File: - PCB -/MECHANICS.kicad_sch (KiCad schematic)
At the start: 7 parts, among them SW1 SW_SPDT, SW3 SW_Push

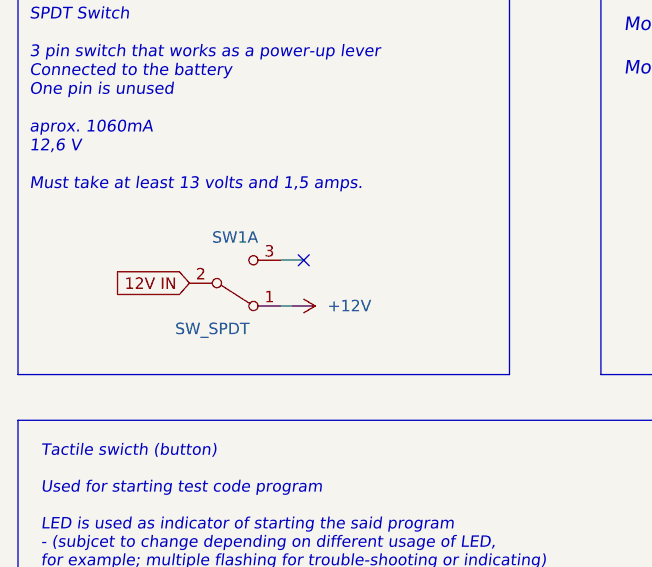
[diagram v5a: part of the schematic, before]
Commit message: PCB almost wired
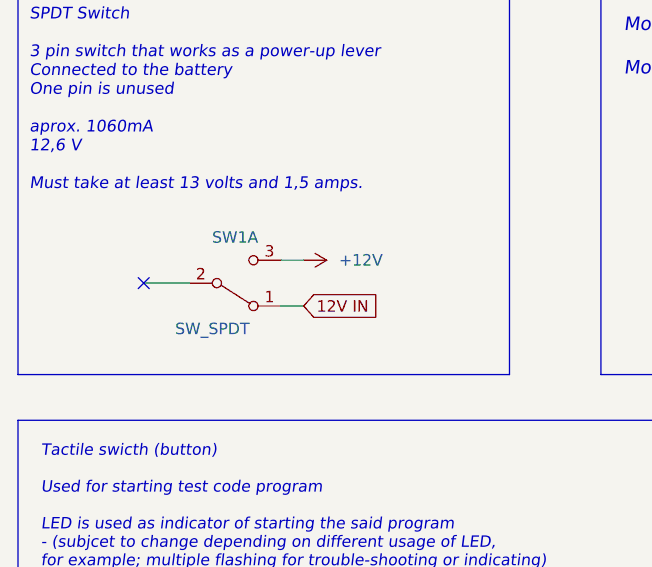
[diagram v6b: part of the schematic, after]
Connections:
- net +12V: now also SW1.3 (C); no longer SW1.1 (A)
- net 12V IN: now also SW1.1 (A); no longer SW1.2 (B)
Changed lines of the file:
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@@
   (junction (at 173.99 139.7) (diameter 0) (color 0 0 0 0)
   )
-  (no_connect (at 97.79 97.79))
+  (no_connect (at 80.01 100.33))
+  (wire (pts (xy 80.01 100.33) (xy 85.09 100.33))
+    (stroke (width 0) (type default))
+  )
   (polyline (pts (xy 66.04 115.57) (xy 218.44 115.57))
     (stroke (width 0) (type default))
@@
     (stroke (width 0) (type default))
   )
+  (wire (pts (xy 95.25 102.87) (xy 97.79 102.87))
+    (stroke (width 0) (type default))
+  )
   (polyline (pts (xy 120.65 67.31) (xy 120.65 110.49))
     (stroke (width 0) (type default))
@@
     (stroke (width 0) (type default))
   )
+  (polyline (pts (xy 68.58 67.31) (xy 120.65 67.31))
+    (stroke (width 0) (type default))
+  )
   (wire (pts (xy 97.79 97.79) (xy 95.25 97.79))
-    (stroke (width 0) (type default))
-  )
-  (polyline (pts (xy 68.58 67.31) (xy 120.65 67.31))
-    (stroke (width 0) (type default))
-  )
-  (wire (pts (xy 96.52 102.87) (xy 95.25 102.87))
     (stroke (width 0) (type default))
   )
@@
     )
   )
-  (global_label "12V IN" (shape input) (at 85.09 100.33 180) (fields_autoplaced)
-    (effects (font (size 1.27 1.27)) (justify right))
-    (property "Intersheetrefs" "${INTERSHEET_REFS}" (at 75.7737 100.33 0)
-      (effects (font (size 1.27 1.27)) (justify right) hide)
+  (global_label "12V IN" (shape input) (at 97.79 102.87 0) (fields_autoplaced)
+    (effects (font (size 1.27 1.27)) (justify left))
+    (property "Intersheetrefs" "${INTERSHEET_REFS}" (at 106.9007 102.87 0)
+      (effects (font (size 1.27 1.27)) (justify left) hide)
     )
   )
@@
     )
   )
-  (symbol (lib_id "power:+12V") (at 96.52 102.87 270) (mirror x) (unit 1)
+  (symbol (lib_id "power:+12V") (at 97.79 97.79 270) (mirror x) (unit 1)
     (in_bom yes) (on_board yes) (dnp no)
-    (property "Reference" "#PWR?" (at 92.71 102.87 0)
-      (effects (font (size 1.27 1.27)) hide)
-    )
-    (property "Value" "+12V" (at 102.87 102.87 90)
-      (effects (font (size 1.27 1.27)))
-    )
-    (property "Footprint" "Battery:BatteryHolder_Bulgin_BX0036_1xC" (at 96.52 102.87 0)
-      (effects (font (size 1.27 1.27)) hide)
-    )
-    (property "Datasheet" "" (at 96.52 102.87 0)
-      (effects (font (size 1.27 1.27)) hide)
-    )
+    (property "Reference" "#PWR?" (at 93.98 97.79 0)
+      (effects (font (size 1.27 1.27)) hide)
+    )
+    (property "Value" "+12V" (at 104.14 97.79 90)
+      (effects (font (size 1.27 1.27)))
+    )
+    (property "Footprint" "Battery:BatteryHolder_Bulgin_BX0036_1xC" (at 97.79 97.79 0)
+      (effects (font (size 1.27 1.27)) hide)
+    )
+    (property "Datasheet" "" (at 97.79 97.79 0)
+      (effects (font (size 1.27 1.27)) hide)
+    )

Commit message: PCB - LED Signal. board upd
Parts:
- removed D1: RLED, LED_THT:LED_D5.0mm, symbol Device:LED
- removed R1: 75, Resistor_THT:R_Axial_DIN0207_L6.3mm_D2.5mm_P10.16mm_Horizontal, symbol Device:R
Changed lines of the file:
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@@
 (kicad_sch (version 20230121) (generator eeschema)
   (paper "A4")
-  (junction (at 173.99 139.7) (diameter 0) (color 0 0 0 0)
-  )
   (no_connect (at 80.01 100.33))
   (wire (pts (xy 80.01 100.33) (xy 85.09 100.33))
@@
     (stroke (width 0) (type default))
   )
-  (wire (pts (xy 193.04 139.7) (xy 194.31 139.7))
-    (stroke (width 0) (type default))
-  )
   (polyline (pts (xy 120.65 110.49) (xy 66.04 110.49))
     (stroke (width 0) (type default))
   )
-  (wire (pts (xy 185.42 139.7) (xy 184.15 139.7))
-    (stroke (width 0) (type default))
-  )
   (polyline (pts (xy 217.17 68.58) (xy 217.17 110.49))
     (stroke (width 0) (type default))
@@
     (stroke (width 0) (type default))
   )
-  (wire (pts (xy 173.99 139.7) (xy 176.53 139.7))
-    (stroke (width 0) (type default))
-  )
   (wire (pts (xy 172.72 139.7) (xy 173.99 139.7))
-    (stroke (width 0) (type default))
-  )
-  (wire (pts (xy 173.99 135.89) (xy 173.99 139.7))
     (stroke (width 0) (type default))
   )
@@
   )
   (text "                 ^\n(subject to change, depending on the LED)\n(different colors have different voltage drop)"
-    (at 167.64 146.05 0)
+    (at 234.95 115.57 0)
     (effects (font (size 1 1) italic) (justify left bottom))
   )
-  (global_label "TEST PROGRAM" (shape input) (at 173.99 135.89 90) (fields_autoplaced)
+  (global_label "TEST PROGRAM" (shape input) (at 173.99 139.7 0) (fields_autoplaced)
     (effects (font (size 1.27 1.27) italic) (justify left))
-    (property "Intersheetrefs" "${INTERSHEET_REFS}" (at 173.99 118.8555 90)
+    (property "Intersheetrefs" "${INTERSHEET_REFS}" (at 191.0245 139.7 0)
       (effects (font (size 1.27 1.27)) (justify left) hide)
     )
@@
     )
   )
-  (symbol (lib_id "power:GND") (at 194.31 139.7 90) (unit 1)
-    (in_bom yes) (on_board yes) (dnp no) (fields_autoplaced)
-    (property "Reference" "#PWR03" (at 200.66 139.7 0)
-      (effects (font (size 1.27 1.27)) hide)
-    )
-    (property "Value" "GND" (at 199.39 139.7 0)
-      (effects (font (size 1.27 1.27)))
-    )
-    (property "Footprint" "" (at 194.31 139.7 0)
-      (effects (font (size 1.27 1.27)) hide)
-    )
-    (property "Datasheet" "" (at 194.31 139.7 0)
-      (effects (font (size 1.27 1.27)) hide)
-    )
-    (pin "1")
-    (instances
-      (project "sumec"
-        (path "/fc70a1a8-ed7c-4a0f-9b1a-f23293528385/05a35bad-c108-46ad-8f95-76319a60a14f"
-          (reference "#PWR03") (unit 1)
-        )
-      )
-    )
-  )
   (symbol (lib_id "Mechanical:MountingHole") (at 138.43 92.71 0) (unit 1)
     (in_bom yes) (on_board yes) (dnp no) (fields_autoplaced)
@@
         (path "/fc70a1a8-ed7c-4a0f-9b1a-f23293528385/05a35bad-c108-46ad-8f95-76319a60a14f"
           (reference "#PWR02") (unit 1)
-        )
-      )
-    )
-  )
-  (symbol (lib_id "Device:R") (at 180.34 139.7 90) (unit 1)
-    (in_bom yes) (on_board yes) (dnp no) (fields_autoplaced)
-    (property "Reference" "R1" (at 179.705 137.16 0)
-      (effects (font (size 1.27 1.27)) (justify left))
-    )
-    (property "Value" "75 " (at 182.245 137.16 0)
-      (effects (font (size 1.27 1.27)) (justify left))
-    )
-    (property "Footprint" "Resistor_THT:R_Axial_DIN0207_L6.3mm_D2.5mm_P10.16mm_Horizontal" (at 180.34 141.478 90)
-      (effects (font (size 1.27 1.27)) hide)
-    )
-    (property "Datasheet" "~" (at 180.34 139.7 0)
-      (effects (font (size 1.27 1.27)) hide)
-    )
-    (pin "1")
-    (pin "2")
-    (instances
-      (project "sumec"
-        (path "/fc70a1a8-ed7c-4a0f-9b1a-f23293528385/05a35bad-c108-46ad-8f95-76319a60a14f"
-          (reference "R1") (unit 1)
         )
       )
@@
         )
       )
-    )
-  )
-  (symbol (lib_id "Device:LED") (at 189.23 139.7 180) (unit 1)
-    (in_bom yes) (on_board yes) (dnp no) (fields_autoplaced)
-    (property "Reference" "D1" (at 190.1825 135.89 90)
-      (effects (font (size 1.27 1.27)) (justify right))
-    )
-    (property "Value" "RLED" (at 192.7225 135.89 90)
-      (effects (font (size 1.27 1.27)) (justify right))
-    )
-    (property "Footprint" "LED_THT:LED_D5.0mm" (at 189.23 139.7 0)
-      (effects (font (size 1.27 1.27)) hide)
-    )
-    (property "Datasheet" "~" (at 189.23 139.7 0)
-      (effects (font (size 1.27 1.27)) hide)
-    )
-    (pin "1")
-    (pin "2")
-    (instances
-      (project "sumec"
-        (path "/fc70a1a8-ed7c-4a0f-9b1a-f23293528385/05a35bad-c108-46ad-8f95-76319a60a14f"
-          (reference "D1") (unit 1)
-        )
-      )

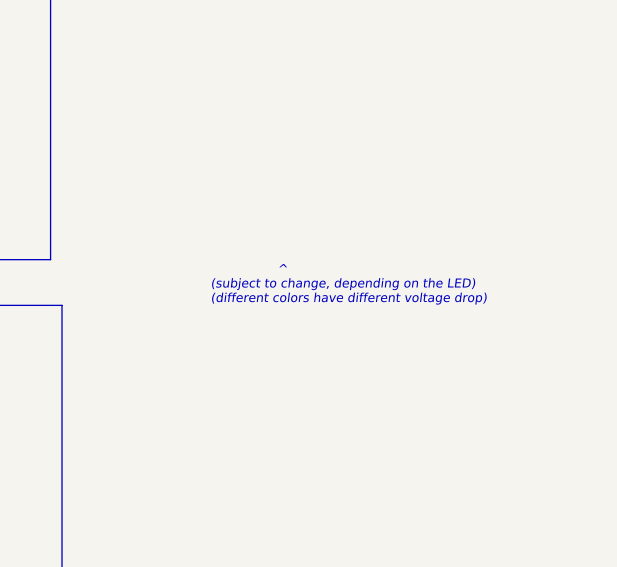
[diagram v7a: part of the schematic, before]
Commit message: PCB - pads update (riveting)
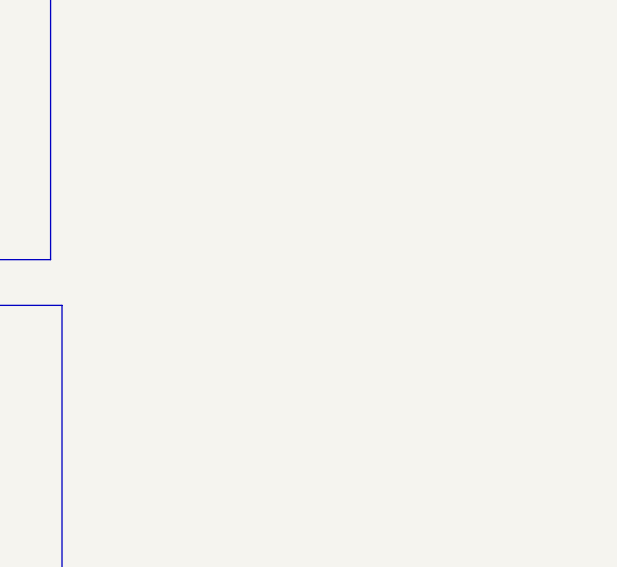
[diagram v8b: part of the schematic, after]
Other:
- note removed: "^ (subject to change, depending on the LED) (different colors have different voltage drop)"
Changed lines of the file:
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@@
     (effects (font (size 1.27 1.27) italic) (justify left bottom))
-  )
-  (text "                 ^\n(subject to change, depending on the LED)\n(different colors have different voltage drop)"
-    (at 234.95 115.57 0)
-    (effects (font (size 1 1) italic) (justify left bottom))
   )
   (global_label "TEST PROGRAM" (shape input) (at 173.99 139.7 0) (fields_autoplaced)
